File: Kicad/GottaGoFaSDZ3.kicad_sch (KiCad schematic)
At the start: 69 parts, among them CN1 Zorro3, J1 Conn_01x06_Male, U1 LM1117-3.3, U10 AS4C32M16SC, U2 74LVCR2245, U3 74LVCR2245, U4 74LVCR2245, U5 74LVCR2245, U6 XC95144XL-TQ100, U7 AS4C32M16SC, U8 AS4C32M16SC, U9 AS4C32M16SC, X1 50MHz

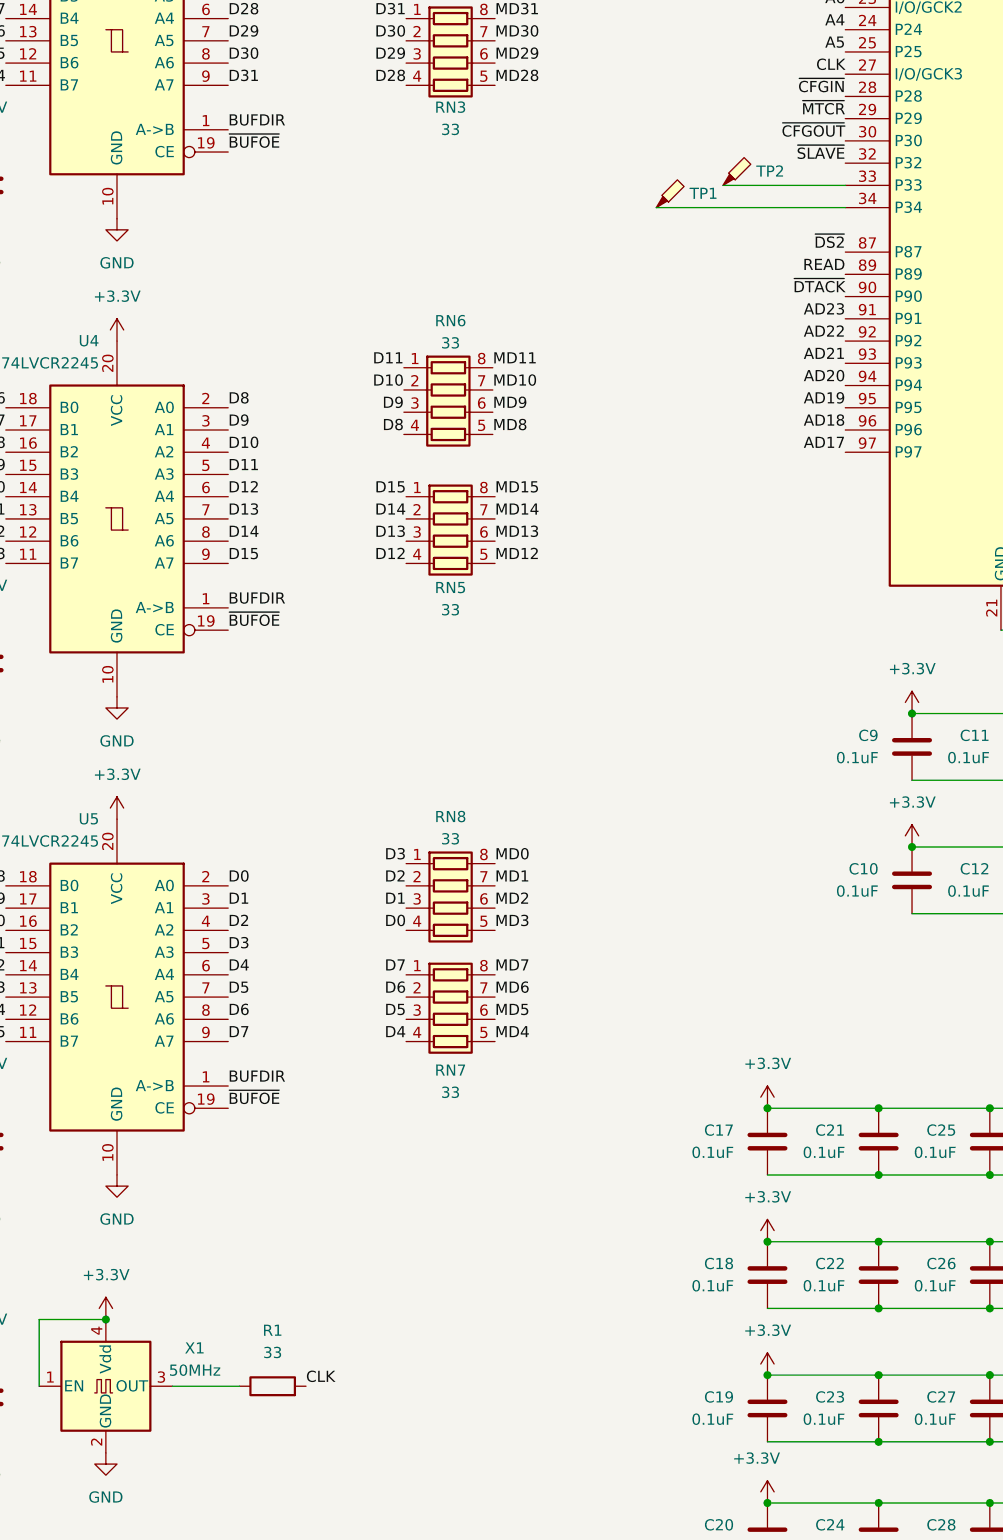
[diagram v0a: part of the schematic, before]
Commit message: Public release
Rev 1A - remove TP1/TP2 and make the board slightly narrower
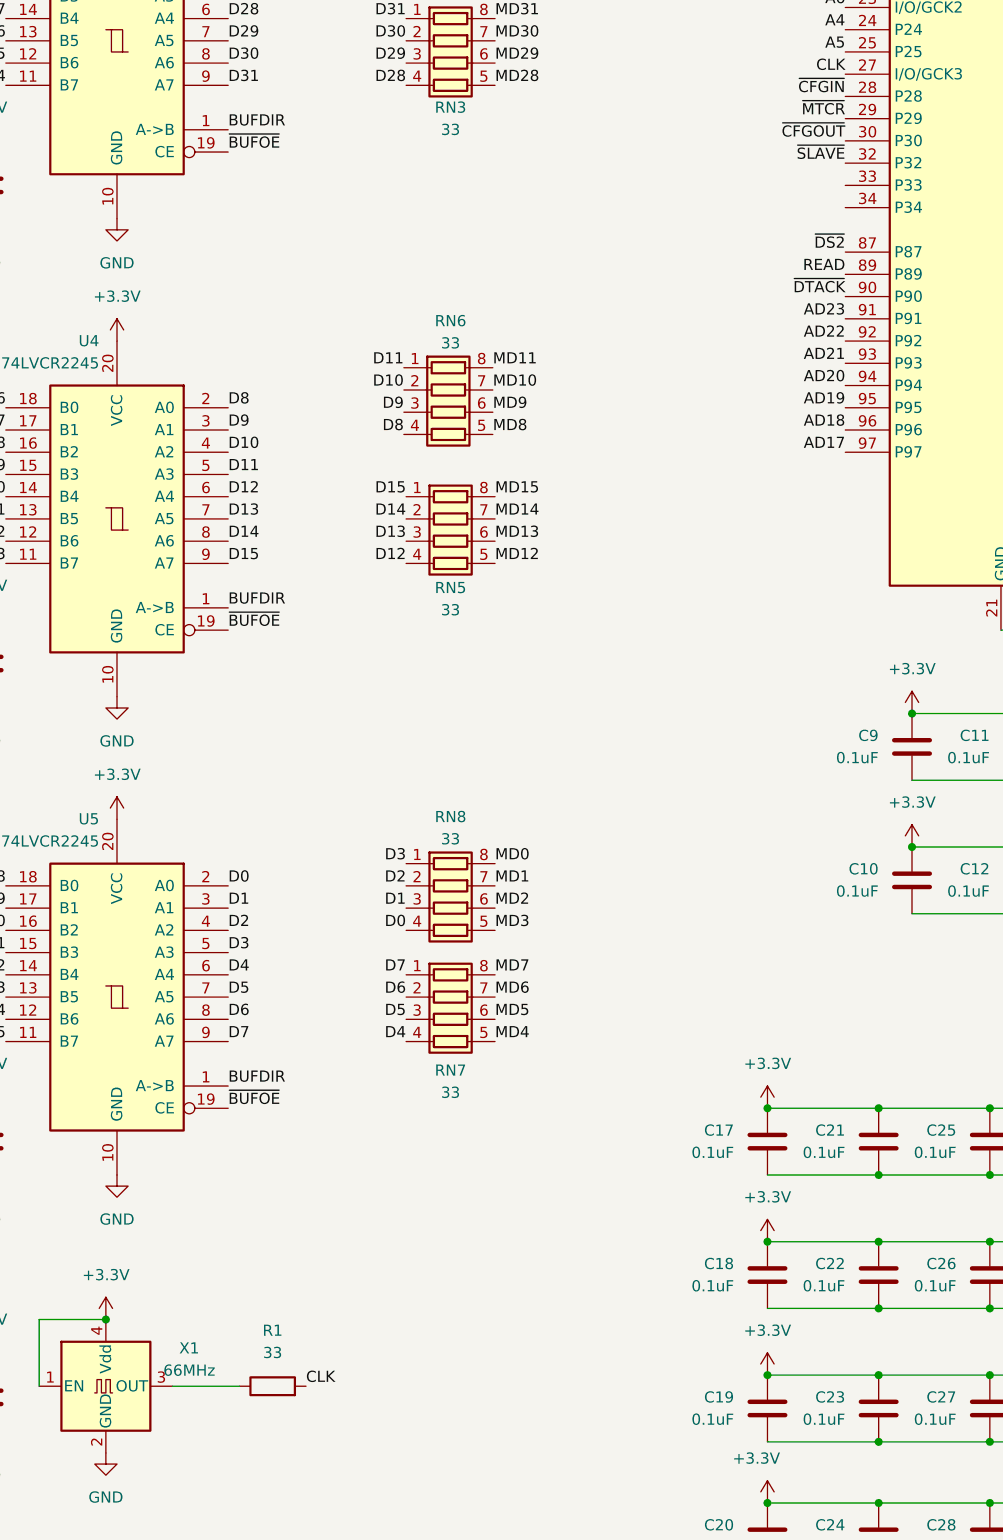
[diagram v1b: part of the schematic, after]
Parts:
- removed TP1, TP2: TestPoint_Probe, TestPoint:TestPoint_THTPad_1.0x1.0mm_Drill0.5mm, symbol Connector:TestPoint_Probe
- X1: value 50MHz -> 66MHz
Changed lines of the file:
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@@
     (stroke (width 0) (type default) (color 0 0 0 0))
   )
-  (wire (pts (xy 185.42 113.03) (xy 199.39 113.03))
-    (stroke (width 0) (type default) (color 0 0 0 0))
-  )
   (wire (pts (xy 229.87 163.83) (xy 232.41 163.83))
     (stroke (width 0) (type default) (color 0 0 0 0))
@@
     (stroke (width 0) (type default) (color 0 0 0 0))
   )
-  (wire (pts (xy 177.8 115.57) (xy 199.39 115.57))
-    (stroke (width 0) (type default) (color 0 0 0 0))
-  )
   (wire (pts (xy 190.5 241.3) (xy 203.2 241.3))
     (stroke (width 0) (type default) (color 0 0 0 0))
@@
     (pin "2")
   )
-  (symbol (lib_id "Connector:TestPoint_Probe") (at 185.42 113.03 0) (unit 1)
-    (in_bom yes) (on_board yes) (fields_autoplaced)
-    (property "Reference" "TP2" (id 0) (at 189.23 111.4424 0)
-      (effects (font (size 1.27 1.27)) (justify left))
-    )
-    (property "Value" "TestPoint_Probe" (id 1) (at 189.23 112.7124 0)
-      (effects (font (size 1.27 1.27)) (justify left) hide)
-    )
-    (property "Footprint" "TestPoint:TestPoint_THTPad_1.0x1.0mm_Drill0.5mm" (id 2) (at 190.5 113.03 0)
-      (effects (font (size 1.27 1.27)) hide)
-    )
-    (property "Datasheet" "~" (id 3) (at 190.5 113.03 0)
-      (effects (font (size 1.27 1.27)) hide)
-    )
-    (pin "1")
-  )
   (symbol (lib_id "power:+3.3V") (at 100.965 109.22 0) (mirror y) (unit 1)
     (in_bom yes) (on_board yes) (fields_autoplaced)
@@
     (pin "2")
   )
-  (symbol (lib_id "Connector:TestPoint_Probe") (at 177.8 115.57 0) (unit 1)
-    (in_bom yes) (on_board yes) (fields_autoplaced)
-    (property "Reference" "TP1" (id 0) (at 181.61 113.9824 0)
-      (effects (font (size 1.27 1.27)) (justify left))
-    )
-    (property "Value" "TestPoint_Probe" (id 1) (at 181.61 115.2524 0)
-      (effects (font (size 1.27 1.27)) (justify left) hide)
-    )
-    (property "Footprint" "TestPoint:TestPoint_THTPad_1.0x1.0mm_Drill0.5mm" (id 2) (at 182.88 115.57 0)
-      (effects (font (size 1.27 1.27)) hide)
-    )
-    (property "Datasheet" "~" (id 3) (at 182.88 115.57 0)
-      (effects (font (size 1.27 1.27)) hide)
-    )
-    (pin "1")
-  )
   (symbol (lib_id "power:+3.3V") (at 116.205 76.2 0) (mirror y) (unit 1)
     (in_bom yes) (on_board yes) (fields_autoplaced)
@@
   (symbol (lib_id "Oscillator:ASV-xxxMHz") (at 114.935 250.19 0) (unit 1)
     (in_bom yes) (on_board yes) (fields_autoplaced)
-    (property "Reference" "X1" (id 0) (at 125.095 245.8593 0))
-    (property "Value" "50MHz" (id 1) (at 125.095 248.3993 0))
+    (property "Reference" "X1" (id 0) (at 124.46 245.8593 0))
+    (property "Value" "66MHz" (id 1) (at 124.46 248.3993 0))
     (property "Footprint" "Oscillator:Oscillator_SMD_Abracon_ASV-4Pin_7.0x5.1mm_HandSoldering" (id 2) (at 132.715 259.08 0)
       (effects (font (size 1.27 1.27)) hide)
@@
       (reference "RN8") (unit 1) (value "33") (footprint "Resistor_SMD:R_Array_Convex_4x0603")
     )
-    (path "/ecc7deac-ddb1-4d03-8dab-eae82aa1e263"
-      (reference "TP1") (unit 1) (value "TestPoint_Probe") (footprint "TestPoint:TestPoint_THTPad_1.0x1.0mm_Drill0.5mm")
-    )
-    (path "/0f1b130f-cef5-4447-8057-c47b2b2fc4de"
-      (reference "TP2") (unit 1) (value "TestPoint_Probe") (footprint "TestPoint:TestPoint_THTPad_1.0x1.0mm_Drill0.5mm")
-    )
     (path "/d230c85c-53c3-4555-8488-5ffe577a6303"
       (reference "U1") (unit 1) (value "LM1117-3.3") (footprint "Package_TO_SOT_SMD:SOT-223-3_TabPin2")
@@
     )
     (path "/ef998be4-742f-4200-840a-09bae2090923"
-      (reference "X1") (unit 1) (value "50MHz") (footprint "Oscillator:Oscillator_SMD_Abracon_ASV-4Pin_7.0x5.1mm_HandSoldering")
+      (reference "X1") (unit 1) (value "66MHz") (footprint "Oscillator:Oscillator_SMD_Abracon_ASV-4Pin_7.0x5.1mm_HandSoldering")
     )
   )

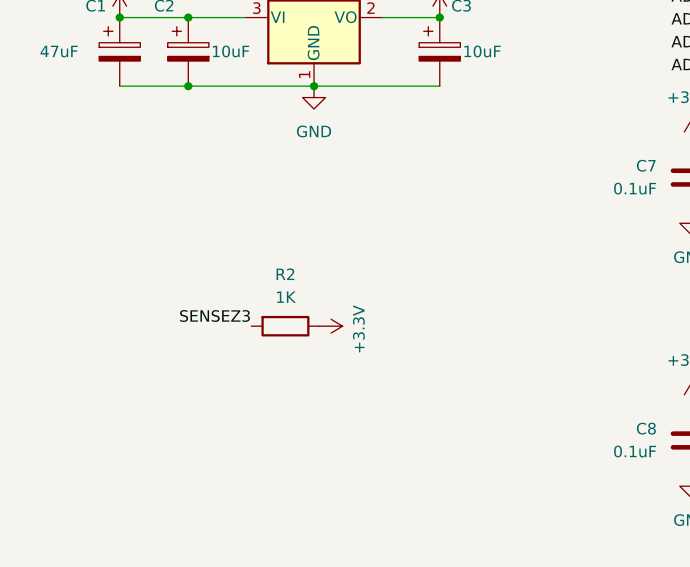
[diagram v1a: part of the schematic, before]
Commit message: Correct R2 value and memory size in README (thanks to Kavanoz)
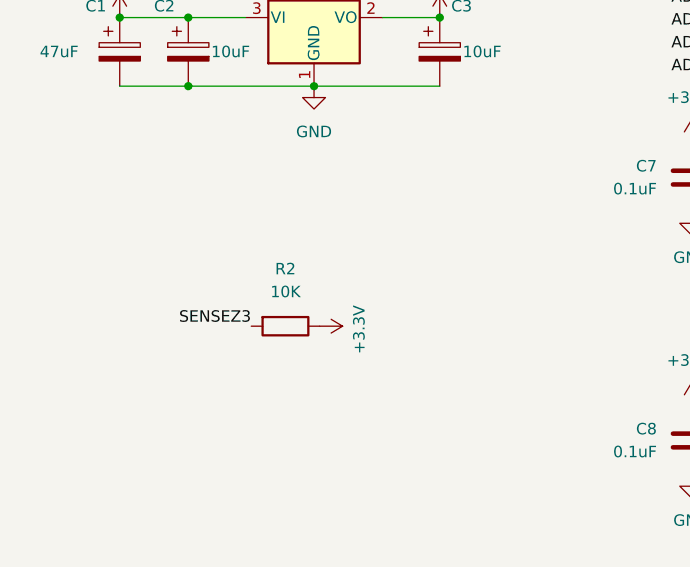
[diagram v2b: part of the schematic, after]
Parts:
- R2: value 1K -> 10K

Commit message: Add reverse install protection
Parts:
- added D1, D2, D3: BAT43W-V, Diode_SMD:D_SOD-123, symbol Diode:BAT43W-V
- added R3, R4: 33, Resistor_SMD:R_0805_2012Metric_Pad1.20x1.40mm_HandSolder, symbol Device:R_Small
- C1: LCSC # (none) -> C239310; Mouser # (none) -> 667-ECE-A1CKA101
- C10, C11, C12, C13, C14, C15, C17, C18, C19, C20, C21, C22, C23, C24, C25, C26, C27, C28, C29, C30, C31, C32, C33, C34, C35, C36, C37, C38, C39, C4, C40, C41, C42, C43, C44, C5, C6, C7, C8, C9: LCSC # (none) -> C14663; Mouser # (none) -> 80-C603C104K5RAC3121
- C16: symbol Device:C -> Device:C_Polarized; LCSC # (none) -> C117023; Mouser # (none) -> 80-T491A106M020
- C2, C3: LCSC # (none) -> C117023; Mouser # (none) -> 80-T491A106M020
- CN1, J1: now left out of the parts list
- R1: LCSC # (none) -> C23140; Mouser # (none) -> 279-CRG0603F33R
- R2: symbol Device:R -> Device:R_Small; LCSC # (none) -> C25804; Mouser # (none) -> 279-CRGH0603J10K
- RN1, RN2, RN3, RN4, RN5, RN6, RN7, RN8: LCSC # (none) -> C25508; Mouser # (none) -> 603-YC164-FR-0733RL
- U1: LCSC # (none) -> C129334; Mouser # (none) -> 926-LM1117IMP3.3NOPB
- U2, U3, U4, U5: LCSC # (none) -> C7848; Mouser # (none) -> 595-SN74LVC245APWT
- U6: LCSC # (none) -> C45126; Mouser # (none) -> 217-5144XL-10TQG100C
- X1: LCSC # (none) -> C387152; Mouser # (none) -> 959-SM7745HEV-66.667
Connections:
- net +3V3: now also C16.1; no longer C16.2
- net DOE: now also D1.1 (K), R3.1; no longer CN1.93 (DOE)
- net GND: now also C16.2, D1.2 (A), D3.2 (A); no longer C16.1
- net SD3: now also D3.1 (K), R4.1; no longer CN1.81 (SD3/D19)
- net SENSEZ3: now also D2.2 (A); no longer CN1.91 (SENSEZ3)
- new net: CN1.93 (DOE), R3.2
- new net: CN1.81 (SD3/D19), R4.2
- new net: CN1.91 (SENSEZ3), D2.1 (K)
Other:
- note added: "Reverse installation protection"
- moved on the sheet: C1, C10, C11, C12, C13, C14, C15, C2, C20, C24, C28, C3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
